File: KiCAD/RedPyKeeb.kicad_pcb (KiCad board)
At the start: 4 copper layers, 347 parts, among them J0 Conn_01x04, J1 Conn_01x04, K0,0 KEYSW, K0,1 KEYSW, K0,2 KEYSW, K0,3 KEYSW, K0,4 KEYSW, K0,5 KEYSW, K1,0 KEYSW, K1,1 KEYSW, K1,2 KEYSW, K1,3 KEYSW, K1,4 KEYSW, K1,5 KEYSW, K10,0 KEYSW, K10,1 KEYSW, K10,2 KEYSW, K10,3 KEYSW, K10,4 KEYSW, K10,5 KEYSW, K11,0 KEYSW, K11,1 KEYSW, K11,2 KEYSW, K11,3 KEYSW, K11,4 KEYSW, K11,5 KEYSW, K12,0 KEYSW, K12,1 KEYSW, K12,2 KEYSW, K12,3 KEYSW, K13,1 KEYSW, K13,2 KEYSW, K14,0 KEYSW, K14,1 KEYSW, K14,3 KEYSW, K14,6 KEYSW, K15,0 KEYSW, K15,1 KEYSW, K15,3 KEYSW, K15,5 KEYSW, K15,6 KEYSW, K16,0 KEYSW, K16,1 KEYSW, K16,3 KEYSW, K16,4 KEYSW, K16,5 KEYSW, K16,6 KEYSW, K17,0 KEYSW, K17,1 KEYSW, K17,3 KEYSW, K17,4 KEYSW, K17,5 KEYSW, K17,6 KEYSW, K18,0 KEYSW, K18,1 KEYSW, K18,3 KEYSW, K18,4 KEYSW, K18,5 KEYSW, K18,6 KEYSW, K19,0 KEYSW, K19,1 KEYSW, K19,3 KEYSW, K19,4 KEYSW, K19,6 KEYSW, K2,0 KEYSW, K2,1 KEYSW, K2,2 KEYSW, K2,3 KEYSW, K2,4 KEYSW, K2,5 KEYSW, K20,0 KEYSW, K20,1 KEYSW, K3,0 KEYSW, K3,1 KEYSW, K3,2 KEYSW, K3,3 KEYSW, K3,4 KEYSW, K3,5 KEYSW, K4,0 KEYSW, K4,1 KEYSW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

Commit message: Update KiCAD files
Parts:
- removed LD13,0, LD20,4, LD20,6, LD4,5, LD5,5, LD6,5, LD7,5: APA102-2020, CrumpPrints:APA102_hand_solder
- C1, C2, C3, D0,0, D0,1, D0,2, D0,3, D0,4, D0,5, D1,0, D1,1, D1,2, D1,3, D1,4, D1,5, D10,0, D10,1, D10,2, D10,3, D10,4, D10,5, D11,0, D11,1, D11,2, D11,3, D11,4, D11,5, D12,0, D12,1, D12,2, D12,3, D13,1, D13,2, D14,0, D14,1, D14,3, D14,6, D15,0, D15,1, D15,3, D15,5, D15,6, D16,0, D16,1, D16,3, D16,4, D16,5, D16,6, D17,0, D17,1, D17,3, D17,4, D17,5, D17,6, D18,0, D18,1, D18,3, D18,4, D18,5, D18,6, D19,0, D19,1, D19,3, D19,4, D19,6, D2,0, D2,1, D2,2, D2,3, D2,4, D2,5, D20,0, D20,1, D3,0, D3,1, D3,2, D3,3, D3,4, D3,5, D4,0, D4,1, D4,2, D4,3, D4,4, D5,0, D5,1, D5,2, D5,3, D5,4, D6,0, D6,1, D6,2, D6,3, D6,4, D7,0, D7,1, D7,2, D7,3, D7,4, D8,0, D8,1, D8,2, D8,3, D8,4, D8,5, D9,0, D9,1, D9,2, D9,3, D9,4, D9,5, J0, J1, U0, U1, U10, U11, U2, U3: moved to B.Cu
- LD0,0, LD0,1, LD0,2, LD0,3, LD0,4, LD0,5, LD1,0, LD1,1, LD1,2, LD1,3, LD1,4, LD1,5, LD10,0, LD10,1, LD10,2, LD10,3, LD10,4, LD10,5, LD11,0, LD11,1, LD11,2, LD11,3, LD11,4, LD11,5, LD12,0, LD12,1, LD12,2, LD12,3, LD13,1, LD13,2, LD14,0, LD14,1, LD14,3, LD14,6, LD15,0, LD15,1, LD15,3, LD15,5, LD15,6, LD16,0, LD16,1, LD16,3, LD16,4, LD16,5, LD16,6, LD17,0, LD17,1, LD17,3, LD17,4, LD17,5, LD17,6, LD17,7, LD18,0, LD18,1, LD18,3, LD18,4, LD18,5, LD18,6, LD18,7, LD19,0, LD19,1, LD19,3, LD19,4, LD19,6, LD19,7, LD2,0, LD2,1, LD2,2, LD2,3, LD2,4, LD2,5, LD20,0, LD20,1, LD20,7, LD3,0, LD3,1, LD3,2, LD3,3, LD3,4, LD3,5, LD4,0, LD4,1, LD4,2, LD4,3, LD4,4, LD5,0, LD5,1, LD5,2, LD5,3, LD5,4, LD6,0, LD6,1, LD6,2, LD6,3, LD6,4, LD7,0, LD7,1, LD7,2, LD7,3, LD7,4, LD8,0, LD8,1, LD8,2, LD8,3, LD8,4, LD8,5, LD9,0, LD9,1, LD9,2, LD9,3, LD9,4, LD9,5: footprint CrumpPrints:APA102_hand_solder -> Custom_pico:LED-APA102-2020; moved to F.Cu
- moved LD20,7 526.0 mm to (603.5, 50.8), turned to 180 degrees
- moved LD19,7 511.4 mm to (578.1, 50.8), turned to 180 degrees
- moved LD20,0 506.3 mm to (603.5, 27.9), turned to 180 degrees
- moved LD19,0 505.4 mm to (578.2, 28.0), turned to 180 degrees
- moved LD20,1 494.9 mm to (603.5, 62.0), turned to 180 degrees
- moved LD18,7 481.0 mm to (552.7, 50.8), turned to 180 degrees
- moved LD18,0 477.7 mm to (552.7, 27.9), turned to 180 degrees
- moved LD19,1 472.1 mm to (578.1, 62.5), turned to 180 degrees
- moved LD19,3 468.4 mm to (578.1, 87.9), turned to 180 degrees
- moved LD19,6 467.6 mm to (603.5, 151.4), turned to 180 degrees
- moved LD18,4 462.4 mm to (578.1, 113.8), turned to 180 degrees
- moved LD16,0 460.9 mm to (496.3, 27.9), turned to 180 degrees
- moved LD17,1 456.1 mm to (527.3, 62.5), turned to 180 degrees
- moved LD19,4 455.1 mm to (603.5, 101.6), turned to 180 degrees
- moved LD17,4 452.7 mm to (552.7, 113.8), turned to 180 degrees
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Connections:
- LD14,0 pad 4: Net-(LD13,0-Pad3) -> Net-(LD12,0-Pad3)
- LD14,0 pad 5: Net-(LD13,0-Pad2) -> Net-(LD12,0-Pad2)
- LD8,5 pad 4: Net-(LD7,5-Pad3) -> Net-(LD3,5-Pad3)
- LD8,5 pad 5: Net-(LD7,5-Pad2) -> Net-(LD3,5-Pad2)
- U2 pad 7: Net-(U2-Pad7) -> KEY_COL20
- U3 pad 1: LED_SCL_ROW0 -> LED_SDA_ROW4
- U3 pad 2: LED_SCL_ROW1 -> LED_SCL_ROW4
- U3 pad 22: LED_SDA_ROW1 -> LED_SCL_ROW0
- U3 pad 23: LED_SDA_ROW2 -> LED_SDA_ROW1
- U3 pad 24: LED_SDA_ROW3 -> LED_SCL_ROW1
- U3 pad 25: LED_SDA_ROW4 -> LED_SDA_ROW2
- U3 pad 26: LED_SDA_ROW5 -> LED_SCL_ROW2
- U3 pad 27: LED_SDA_ROW6 -> LED_SDA_ROW3
- U3 pad 28: LED_SDA_ROW7 -> LED_SCL_ROW3
- U3 pad 3: LED_SCL_ROW2 -> LED_SDA_ROW5
- U3 pad 4: LED_SCL_ROW3 -> LED_SCL_ROW5
- U3 pad 5: LED_SCL_ROW4 -> LED_SDA_ROW6
- U3 pad 6: LED_SCL_ROW5 -> LED_SCL_ROW6
- U3 pad 7: LED_SCL_ROW6 -> LED_SDA_ROW7
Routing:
- net MAIN_VBUS: track 221.0 -> 1106.5 mm, vias 5 -> 6
- net GNDPWR: track 211.2 -> 854.2 mm, vias 7 -> 4
- net KEY_ROW6: track 165.9 -> 705.4 mm
- net IO_INT0: track 9.86 -> 424.1 mm, vias 0 -> 2
- net IO_INT1: track 14.4 -> 425.5 mm, vias 0 -> 2
- net I2C_SCL0: track 81.8 -> 467.5 mm
- net I2C_SDA0: track 80.4 -> 461.0 mm
- net KEY_COL6: track 145.6 -> 340.7 mm, vias 0 -> 6
- net KEY_ROW4: track 554.8 -> 732.4 mm
- net KEY_ROW5: track 535.3 -> 706.1 mm
- net KEY_COL5: track 148.9 -> 318.7 mm, vias 0 -> 6
- net KEY_COL4: track 135.4 -> 264.8 mm, vias 0 -> 6
- net KEY_COL11: track 208.4 -> 319.0 mm, vias 0 -> 6
- net KEY_COL3: track 201.9 -> 306.2 mm, vias 0 -> 7
- net KEY_ROW2: track 342.9 -> 430.6 mm
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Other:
- board outline added: 594.9 x 162.6 mm

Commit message: Update KiCAD files
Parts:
- turned LD2,2 to 180 degrees
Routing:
- net GNDPWR: track 854.2 -> 4166.0 mm, vias 4 -> 7
- net MAIN_VBUS: track 1106.5 -> 4094.0 mm, vias 6 -> 7
- net KEY_ROW4: track 732.4 -> 559.4 mm
- net Net-(LD11,4-Pad2): track 0.00 -> 155.6 mm
- net Net-(LD11,4-Pad3): track 0.00 -> 154.4 mm
- net Net-(LD2,5-Pad3): track 0.00 -> 95.3 mm
- net Net-(LD2,5-Pad2): track 0.00 -> 95.3 mm
- net Net-(LD3,5-Pad3): track 0.00 -> 84.2 mm
- net Net-(LD3,5-Pad2): track 0.00 -> 84.2 mm
- net Net-(LD11,5-Pad3): track 0.00 -> 78.9 mm
- net Net-(LD11,5-Pad2): track 0.00 -> 78.5 mm
- net Net-(LD12,3-Pad3): track 0.00 -> 61.7 mm
- net Net-(LD12,3-Pad2): track 0.00 -> 61.2 mm
- net Net-(LD15,5-Pad2): track 0.00 -> 55.0 mm
- net Net-(LD15,5-Pad3): track 0.00 -> 55.0 mm
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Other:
- outline, holes or cut-outs redrawn

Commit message: Update KiCAD files
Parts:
- C3, U3: moved to F.Cu
- C6: moved to B.Cu
- moved U0 452.4 mm to (23.7, 5.27), turned to 90 degrees
- moved U11 430.0 mm to (9.65, 17.3), turned to 270 degrees
- moved C2 408.9 mm to (14.7, 28.6)
- moved U2 407.2 mm to (14.2, 40.8)
- moved U10 405.2 mm to (19.8, 17.3), turned to 270 degrees
- moved C6 400.9 mm to (84.8, 9.14), turned to 0 degrees
- moved J1 395.2 mm to (82.5, -14.7)
- moved J0 380.7 mm to (82.5, -0.83), turned to 90 degrees
- moved LD19,6 144.7 mm to (460.9, 127.1)
- moved K19,6 144.7 mm to (460.6, 131.9)
- moved K19,4 143.7 mm to (460.6, 93.1)
- moved LD19,4 143.7 mm to (460.6, 86.5)
- moved LD20,0 143.3 mm to (460.5, 19.4)
- moved K20,0 143.2 mm to (460.5, 26.2)
- moved K20,1 143.0 mm to (460.6, 64.2)
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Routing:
- net GNDPWR: track 4166.0 -> 2918.7 mm, vias 7 -> 5
- net MAIN_VBUS: track 4094.0 -> 3022.0 mm, vias 7 -> 10
- net LED_SCL_ROW7: track 0.00 -> 590.9 mm, vias 0 -> 4
- net LED_SDA_ROW7: track 0.00 -> 589.6 mm, vias 0 -> 2
- net KEY_COL20: track 35.6 -> 558.3 mm
- net KEY_COL19: track 141.4 -> 621.8 mm, vias 5 -> 2
- net KEY_COL18: track 150.8 -> 605.3 mm, vias 6 -> 2
- net KEY_COL17: track 154.1 -> 591.4 mm, vias 6 -> 2
- net KEY_COL16: track 171.1 -> 592.9 mm, vias 6 -> 2
- net LED_SCL_ROW6: track 0.00 -> 417.8 mm, vias 0 -> 2
- net LED_SDA_ROW6: track 0.00 -> 410.1 mm, vias 0 -> 2
- net I2C_SCL0: track 467.5 -> 59.1 mm
- net I2C_SDA0: track 461.0 -> 60.3 mm, vias 4 -> 3
- net IO_INT0: track 424.1 -> 46.6 mm
- net IO_INT1: track 425.5 -> 50.7 mm
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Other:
- board size 594.9 x 162.6 mm -> 482.6 x 183.4 mm

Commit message: Update KiCAD files, hopefully a working board this time.
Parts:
- moved D11,5 87.7 mm to (352.6, 207.4)
- moved D12,2 87.7 mm to (326.1, 148.8)
- moved D12,3 87.7 mm to (343.2, 168.3)
- moved D13,1 87.7 mm to (345.1, 129.5)
- moved D13,2 87.7 mm to (350.0, 148.8)
- moved D14,6 87.7 mm to (383.1, 207.3)
- moved D15,1 87.7 mm to (402.5, 129.5)
- moved D15,3 87.7 mm to (402.5, 148.8)
- moved D16,3 87.7 mm to (422.0, 148.8)
- moved D16,5 87.7 mm to (454.5, 187.5)
- moved D16,6 87.7 mm to (421.7, 207.3)
- moved D17,0 87.7 mm to (454.7, 91.5)
- moved D17,6 87.7 mm to (464.6, 206.9)
- moved D19,0 87.7 mm to (493.3, 91.5)
- moved D9,1 87.7 mm to (258.2, 129.6)
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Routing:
- net MAIN_VBUS: track 3022.0 -> 4475.6 mm, vias 10 -> 47
- net GNDPWR: track 2918.7 -> 3226.7 mm, vias 5 -> 6
- net KEY_COL4: track 117.0 -> 218.5 mm
- net KEY_COL11: track 445.3 -> 449.1 mm
- net KEY_COL17: track 591.4 -> 594.2 mm
- net KEY_COL6: track 269.3 -> 272.1 mm
- net KEY_COL10: track 425.7 -> 428.2 mm
- net Net-(D2,4-Pad2): track 0.00 -> 1.98 mm
- net KEY_COL16: track 592.9 -> 594.8 mm
- net KEY_COL3: track 252.0 -> 253.4 mm
- net KEY_COL5: track 248.5 -> 249.8 mm
- net KEY_COL9: track 404.1 -> 404.9 mm

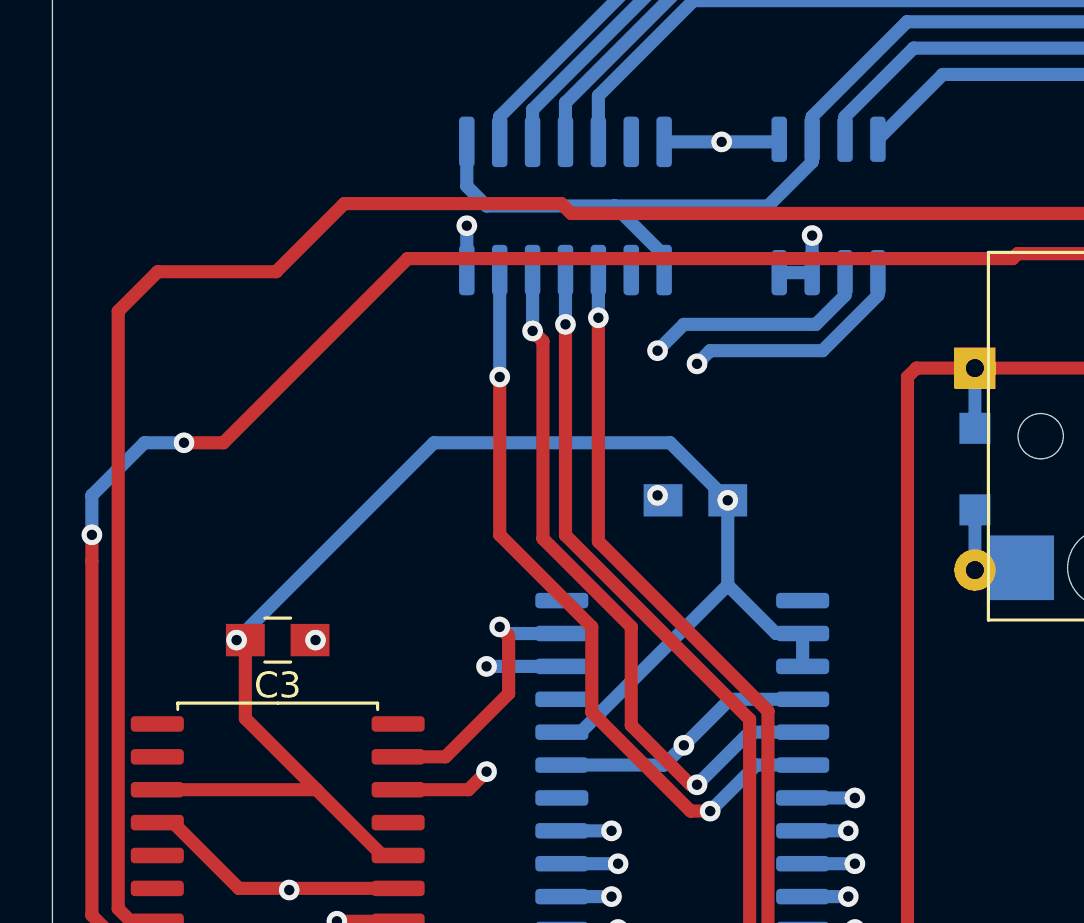
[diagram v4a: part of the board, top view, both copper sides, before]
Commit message: Update KiCAD files to fix minor issues. Add initial release of firmware, not currently functioning.
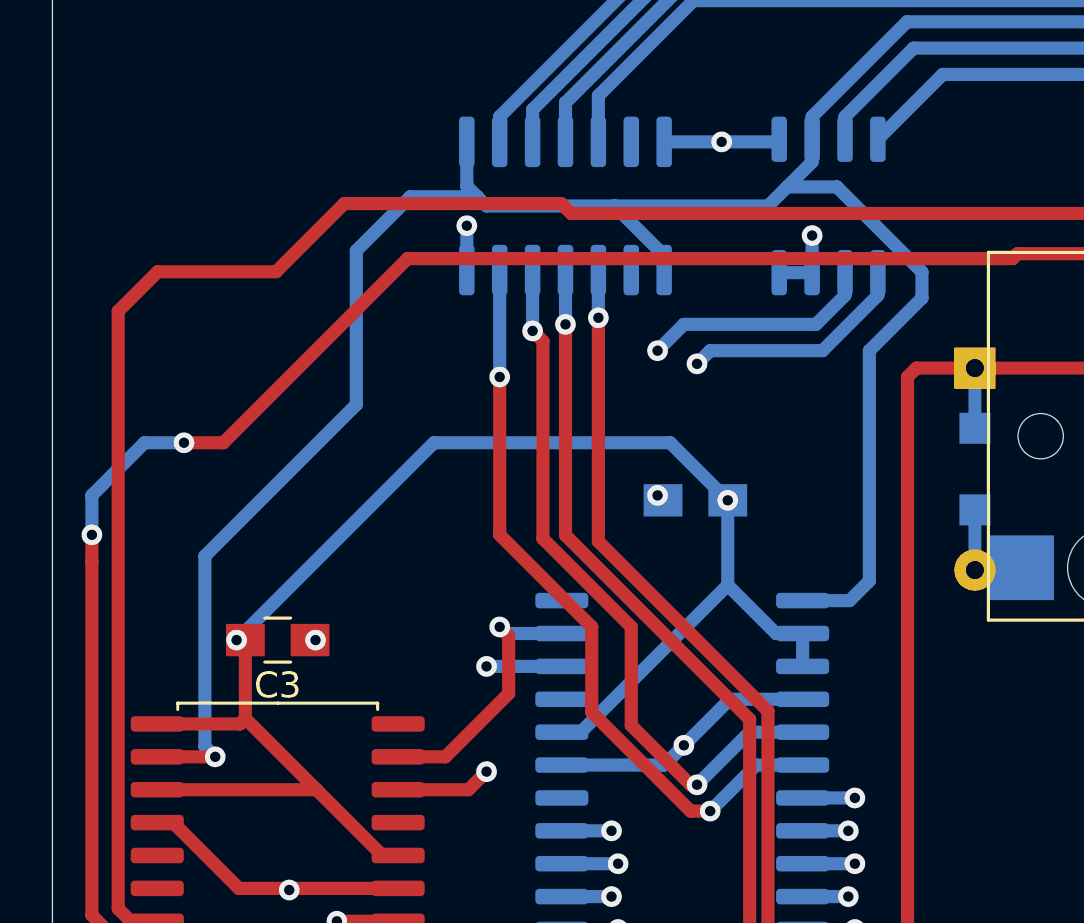
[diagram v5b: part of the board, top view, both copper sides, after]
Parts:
- D12,2: value D -> BAT54W-HG3-18
- U1, U2, U3: value MCP23017_SO -> MCP23017-E/SO
- U10: value PCA9306D -> PCA9306DP
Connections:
- U2 pad 15: Net-(U2-Pad15) -> PICO_33_REF
- U3 pad 15: Net-(U3-Pad15) -> GNDPWR
- U3 pad 16: Net-(U3-Pad16) -> PICO_33_REF
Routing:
- net PICO_33_REF: track 72.9 -> 125.0 mm, vias 0 -> 1
- net GNDPWR: track 3226.7 -> 3230.2 mm
- net MAIN_VBUS: track 4475.6 -> 4476.7 mm

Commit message: Update KiCAD files.
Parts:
- added C4: 0805B101K100CT, Capacitor_SMD:C_0805_2012Metric_Pad1.18x1.45mm_HandSolder, B.Cu at (452.6, 82.5)
- added C5: 0805B101K100CT, Capacitor_SMD:C_0805_2012Metric_Pad1.18x1.45mm_HandSolder, B.Cu at (438.0, 80.3)
- added C7: 0805B101K100CT, Capacitor_SMD:C_0805_2012Metric_Pad1.18x1.45mm_HandSolder, B.Cu at (438.1, 75.0)
- added J2: Conn_01x04, Connector_JST:JST_EH_S4B-EH_1x04_P2.50mm_Horizontal, F.Cu at (442.1, 51.3)
- added R1: APC0805B1K00N, Resistors_SMD:R_0805_HandSoldering, B.Cu at (458.1, 81.9)
- added R2: APC0805B1K00N, Resistors_SMD:R_0805_HandSoldering, B.Cu at (460.1, 81.9)
- added R3: ERJ-6RED2003V, Resistors_SMD:R_0805_HandSoldering, B.Cu at (460.2, 78.5)
- added R4: APC0805B1K00N, Resistors_SMD:R_0805_HandSoldering, B.Cu at (458.5, 74.0)
- added R5: APC0805B1K00N, Resistors_SMD:R_0805_HandSoldering, B.Cu at (456.6, 74.0)
- C1, C2: moved to F.Cu
- C3: moved to B.Cu
- C6: value EEE-FK1A102AL -> EEE-FN1C102UV
- D0,0, D0,1, D0,2, D0,3, D0,4, D0,5, D1,0, D1,1, D1,2, D1,3, D1,4, D1,5, D10,0, D10,1, D10,2, D10,3, D10,4, D10,5, D11,0, D11,1, D11,2, D11,3, D11,4, D11,5, D12,0, D12,1, D12,3, D13,1, D13,2, D14,0, D14,1, D14,3, D14,6, D15,0, D15,1, D15,3, D15,5, D15,6, D16,0, D16,1, D16,3, D16,4, D16,5, D16,6, D17,0, D17,1, D17,3, D17,4, D17,5, D17,6, D18,0, D18,1, D18,3, D18,4, D18,5, D18,6, D19,0, D19,1, D19,3, D19,4, D19,6, D2,0, D2,1, D2,2, D2,3, D2,4, D2,5, D20,0, D20,1, D3,0, D3,1, D3,2, D3,3, D3,4, D3,5, D4,0, D4,1, D4,2, D4,3, D4,4, D5,0, D5,1, D5,2, D5,3, D5,4, D6,0, D6,1, D6,2, D6,3, D6,4, D7,0, D7,1, D7,2, D7,3, D7,4, D8,0, D8,1, D8,2, D8,3, D8,4, D8,5, D9,0, D9,1, D9,2, D9,3, D9,4, D9,5: value D -> BAT54W-HG3-08
- K0,0, K0,1, K0,2, K0,3, K0,4, K0,5, K1,0, K1,1, K1,2, K1,3, K1,4, K1,5, K10,0, K10,1, K10,2, K10,3, K10,4, K10,5, K11,0, K11,1, K11,2, K11,3, K11,4, K11,5, K12,0, K12,1, K12,2, K12,3, K13,1, K13,2, K14,0, K14,1, K14,3, K14,6, K15,0, K15,1, K15,3, K15,5, K15,6, K16,0, K16,1, K16,3, K16,4, K16,5, K16,6, K17,0, K17,1, K17,3, K17,4, K17,5, K17,6, K18,0, K18,1, K18,3, K18,4, K18,5, K18,6, K19,0, K19,1, K19,3, K19,4, K19,6, K2,0, K2,1, K2,2, K2,3, K2,4, K2,5, K20,0, K20,1, K3,0, K3,1, K3,2, K3,3, K3,4, K3,5, K4,0, K4,1, K4,2, K4,3, K4,4, K5,0, K5,1, K5,2, K5,3, K5,4, K6,0, K6,1, K6,2, K6,3, K6,4, K7,0, K7,1, K7,2, K7,3, K7,4, K8,0, K8,1, K8,2, K8,3, K8,4, K8,5, K9,0, K9,1, K9,2, K9,3, K9,4, K9,5: value KEYSW -> ~
- LD0,0, LD0,1, LD0,2, LD0,3, LD0,4, LD0,5, LD1,0, LD1,1, LD1,2, LD1,3, LD1,4, LD1,5, LD10,0, LD10,1, LD10,2, LD10,3, LD10,4, LD10,5, LD11,0, LD11,1, LD11,2, LD11,3, LD11,4, LD11,5, LD12,0, LD12,1, LD12,2, LD12,3, LD13,1, LD13,2, LD14,0, LD14,1, LD14,3, LD14,6, LD15,0, LD15,1, LD15,3, LD15,5, LD15,6, LD16,0, LD16,1, LD16,3, LD16,4, LD16,5, LD16,6, LD17,0, LD17,1, LD17,3, LD17,4, LD17,5, LD17,6, LD17,7, LD18,0, LD18,1, LD18,3, LD18,4, LD18,5, LD18,6, LD18,7, LD19,0, LD19,1, LD19,3, LD19,4, LD19,6, LD19,7, LD2,0, LD2,1, LD2,2, LD2,3, LD2,4, LD2,5, LD20,0, LD20,1, LD20,7, LD3,0, LD3,1, LD3,2, LD3,3, LD3,4, LD3,5, LD4,0, LD4,1, LD4,2, LD4,3, LD4,4, LD5,0, LD5,1, LD5,2, LD5,3, LD5,4, LD6,0, LD6,1, LD6,2, LD6,3, LD6,4, LD7,0, LD7,1, LD7,2, LD7,3, LD7,4, LD8,0, LD8,1, LD8,2, LD8,3, LD8,4, LD8,5, LD9,0, LD9,1, LD9,2, LD9,3, LD9,4, LD9,5: value APA102-2020 -> APA102 2020
- U0: value USB_Pico -> ~
- U10: value PCA9306DP -> PCA9306DQER; footprint Package_SO:SO-8_3.9x4.9mm_P1.27mm -> Package_SO:SSOP-8_2.95x2.8mm_P0.65mm
- moved U10 375.7 mm to (455.4, 79.4)
- moved U11 374.3 mm to (443.8, 78.7)
- moved U0 348.4 mm to (431.9, 67.1)
- moved C6 346.7 mm to (491.4, 73.0)
- moved J0 344.5 mm to (486.9, 60.4)
- moved J1 339.7 mm to (480.7, 80.6), turned to 180 degrees
- moved C2 334.7 mm to (409.2, 84.2)
- moved U2 332.3 mm to (405.7, 84.3), turned to 270 degrees
- moved U1 36.6 mm to (107.4, 112.3), turned to 180 degrees
- moved U3 34.5 mm to (83.8, 86.1), turned to 270 degrees
- moved C1 33.6 mm to (107.8, 114.3), turned to 270 degrees
- moved C3 24.8 mm to (80.4, 86.5)
- moved K20,0 22.7 mm to (501.3, 102.5)
- moved LD20,0 22.7 mm to (501.3, 95.7)
- moved D17,0 22.7 mm to (435.6, 103.7)
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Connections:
- U10 pad 7: MAIN_VBUS -> Net-(C4-Pad2)
- U10 pad 8: MAIN_VBUS -> Net-(C4-Pad2)
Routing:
- net MAIN_VBUS: track 4476.7 -> 4998.0 mm, vias 47 -> 57
- net KEY_COL16: track 594.8 -> 181.5 mm
- net KEY_COL20: track 558.3 -> 149.0 mm
- net KEY_COL19: track 621.8 -> 214.2 mm
- net KEY_COL18: track 605.4 -> 200.1 mm
- net KEY_COL17: track 594.2 -> 190.0 mm
- net I2C_SDA0: track 60.3 -> 450.4 mm, vias 3 -> 5
- net I2C_SCL0: track 59.1 -> 447.0 mm, vias 4 -> 5
- net GNDPWR: track 3230.2 -> 3610.8 mm, vias 6 -> 9
- net PICO_33_REF: track 125.0 -> 497.8 mm, vias 1 -> 3
- net KEY_COL15: track 527.8 -> 178.2 mm
- net IO_INT0: track 46.6 -> 371.8 mm, vias 2 -> 4
- net KEY_COL14: track 507.4 -> 187.7 mm
- net IO_INT1: track 50.7 -> 367.3 mm, vias 2 -> 4
- net KEY_COL12: track 406.3 -> 146.0 mm, vias 2 -> 0
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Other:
- board size 482.6 x 183.4 mm -> 448.3 x 179.1 mm
- net class USB added: clearance 0.2, trace_width 0.4, via_dia 0.8, via_drill 0.4

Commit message: Update firmware and KiCAD files.
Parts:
- D12,2: value BAT54W-HG3-18 -> BAT54W-HG3-08
- J2: footprint Connector_JST:JST_EH_S4B-EH_1x04_P2.50mm_Horizontal -> Connector_JST:JST_EH_S7B-EH_1x07_P2.50mm_Horizontal
- U10: value PCA9306DQER -> PCA9306DP
- moved J2 2.95 mm to (445.0, 50.9)
- moved LD13,2 1.03 mm to (353.3, 140.7)
- moved LD0,4 1.03 mm to (100.2, 179.9)
- moved LD19,1 0.50 mm to (482.1, 121.5)
- moved LD0,2 0.35 mm to (93.1, 140.7)
- moved LD19,0 0.24 mm to (482.0, 95.6)
- moved LD17,0 0.12 mm to (443.4, 95.6)
- moved LD18,0 0.12 mm to (462.7, 95.6)
- moved LD20,0 0.11 mm to (501.3, 95.6)
- moved LD17,3 0.10 mm to (443.5, 140.7)
- moved LD18,3 0.10 mm to (462.8, 140.7)
- moved LD19,3 0.10 mm to (482.1, 140.7)
- moved LD0,0 0.08 mm to (88.5, 95.5)
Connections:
- U0 pad 21: Net-(J2-Pad4) -> Net-(U0-Pad21)
- U0 pad 22: Net-(J2-Pad3) -> Net-(J2-Pad5)
- U0 pad 24: Net-(J2-Pad2) -> Net-(J2-Pad3)
- U0 pad 25: Net-(J2-Pad1) -> Net-(J2-Pad4)
- U0 pad 26: Net-(U0-Pad26) -> Net-(J2-Pad6)
- U0 pad 27: Net-(U0-Pad27) -> Net-(J2-Pad7)
- U0 pad 36: Net-(U0-Pad36) -> Net-(J2-Pad1)
- U0 pad 38: Net-(U0-Pad38) -> Net-(J2-Pad2)
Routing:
- net MAIN_VBUS: track 4998.0 -> 4783.6 mm, vias 57 -> 56
- net GNDPWR: track 3610.8 -> 3540.1 mm
- net Net-(J2-Pad2): track 4.13 -> 37.3 mm
- net Net-(J2-Pad7): track 0.00 -> 28.9 mm
- net Net-(J2-Pad1): track 4.82 -> 29.0 mm
- net Net-(J2-Pad6): track 0.00 -> 24.1 mm
- net Net-(LD16,3-Pad2): track 30.4 -> 22.2 mm
- net Net-(J2-Pad5): track 0.00 -> 3.54 mm
- net Net-(J2-Pad4): track 4.11 -> 7.24 mm
- net Net-(LD17,0-Pad3): track 16.2 -> 17.6 mm
- net Net-(LD14,3-Pad3): track 16.2 -> 17.6 mm
- net Net-(LD14,1-Pad3): track 16.2 -> 17.6 mm
- net Net-(LD10,5-Pad4): track 21.1 -> 22.5 mm
- net Net-(LD7,2-Pad3): track 16.2 -> 17.6 mm
- net Net-(LD18,6-Pad3): track 19.6 -> 21.0 mm
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
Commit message: Update KiCAD files.
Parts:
- U10: value PCA9306DP -> PCA9306DP,118; footprint Package_SO:SSOP-8_2.95x2.8mm_P0.65mm -> Package_SO:TSSOP-8_3x3mm_P0.65mm
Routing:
- net MAIN_VBUS: track 4783.6 -> 4795.4 mm
- net GNDPWR: track 3540.1 -> 3543.4 mm
